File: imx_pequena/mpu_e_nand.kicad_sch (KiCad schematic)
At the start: 1 part, among them U1 MCIMX6Z0DVM09AB

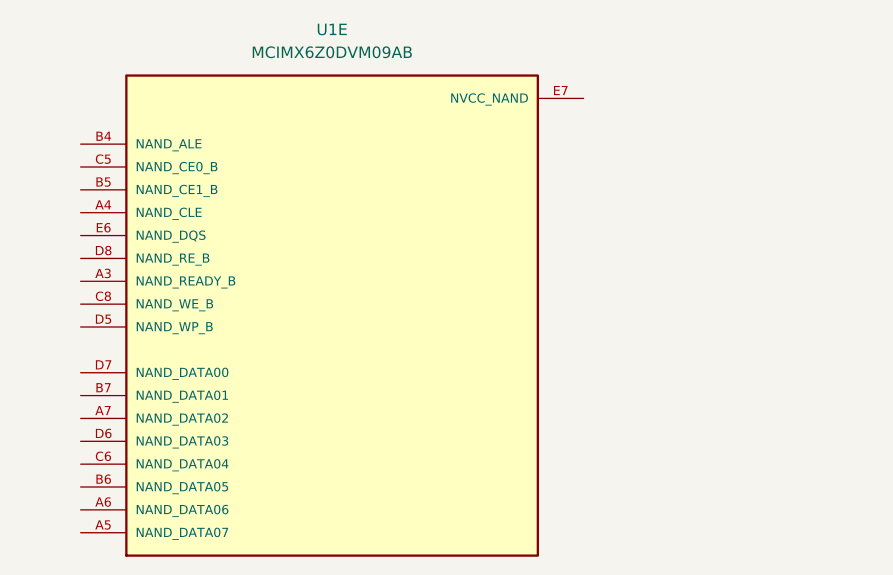
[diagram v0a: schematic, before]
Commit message: Cleaned up NVCC pins
Added 3v3 connections + decoupling caps to NVcc pins
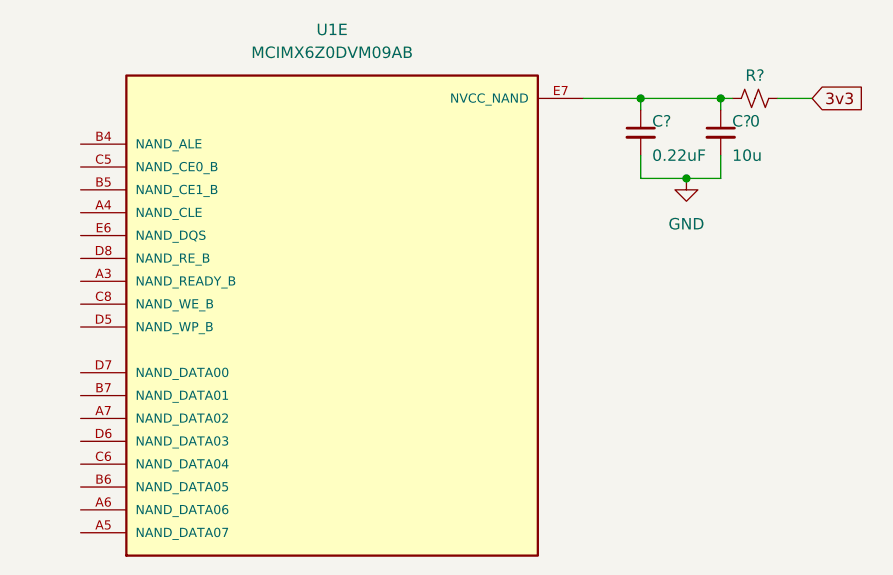
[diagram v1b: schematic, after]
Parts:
- added C?: 10u, symbol Device:C_Small
- added C?: 0.22uF, symbol Device:C_Small
- added R?: 0, symbol Device:R_Small_US
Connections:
- net at U1.E7 (NVCC_NAND): now also C?.1, C?.1, R?.1
- new net 3v3: R?.2
- new net GND: C?.2, C?.2
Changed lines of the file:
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@@
 (kicad_sch (version 20211123) (generator eeschema)
   (paper "A4")
+  (junction (at 181.61 63.5) (diameter 0) (color 0 0 0 0)
+  )
+  (junction (at 190.5 63.5) (diameter 0) (color 0 0 0 0)
+  )
+  (junction (at 186.69 72.39) (diameter 0) (color 0 0 0 0)
+  )
+  (wire (pts (xy 190.5 69.85) (xy 190.5 72.39))
+    (stroke (width 0) (type default) (color 0 0 0 0))
+  )
+  (wire (pts (xy 190.5 63.5) (xy 191.77 63.5))
+    (stroke (width 0) (type default) (color 0 0 0 0))
+  )
+  (wire (pts (xy 190.5 63.5) (xy 190.5 64.77))
+    (stroke (width 0) (type default) (color 0 0 0 0))
+  )
+  (wire (pts (xy 181.61 63.5) (xy 181.61 64.77))
+    (stroke (width 0) (type default) (color 0 0 0 0))
+  )
+  (wire (pts (xy 181.61 63.5) (xy 190.5 63.5))
+    (stroke (width 0) (type default) (color 0 0 0 0))
+  )
+  (wire (pts (xy 175.26 63.5) (xy 181.61 63.5))
+    (stroke (width 0) (type default) (color 0 0 0 0))
+  )
+  (wire (pts (xy 186.69 72.39) (xy 190.5 72.39))
+    (stroke (width 0) (type default) (color 0 0 0 0))
+  )
+  (wire (pts (xy 181.61 72.39) (xy 186.69 72.39))
+    (stroke (width 0) (type default) (color 0 0 0 0))
+  )
+  (wire (pts (xy 196.85 63.5) (xy 200.66 63.5))
+    (stroke (width 0) (type default) (color 0 0 0 0))
+  )
+  (wire (pts (xy 181.61 69.85) (xy 181.61 72.39))
+    (stroke (width 0) (type default) (color 0 0 0 0))
+  )
+  (global_label "3v3" (shape input) (at 200.66 63.5 0) (fields_autoplaced)
+    (effects (font (size 1.27 1.27)) (justify left))
+    (property "Intersheet References" "${INTERSHEET_REFS}" (id 0) (at 206.4598 63.4206 0)
+      (effects (font (size 1.27 1.27)) (justify left) hide)
+    )
+  )
+  (symbol (lib_id "Device:C_Small") (at 190.5 67.31 0) (unit 1)
+    (in_bom yes) (on_board yes)
+    (property "Reference" "C?" (id 0) (at 191.77 66.04 0)
+      (effects (font (size 1.27 1.27)) (justify left))
+    )
+    (property "Value" "10u" (id 1) (at 191.77 69.85 0)
+      (effects (font (size 1.27 1.27)) (justify left))
+    )
+    (property "Footprint" "" (id 2) (at 190.5 67.31 0)
+      (effects (font (size 1.27 1.27)) hide)
+    )
+    (property "Datasheet" "~" (id 3) (at 190.5 67.31 0)
+      (effects (font (size 1.27 1.27)) hide)
+    )
+    (pin "1")
+    (pin "2")
+  )
+  (symbol (lib_id "Device:R_Small_US") (at 194.31 63.5 90) (unit 1)
+    (in_bom yes) (on_board yes)
+    (property "Reference" "R?" (id 0) (at 194.31 60.96 90))
+    (property "Value" "0" (id 1) (at 194.31 66.04 90))
+    (property "Footprint" "" (id 2) (at 194.31 63.5 0)
+      (effects (font (size 1.27 1.27)) hide)
+    )
+    (property "Datasheet" "~" (id 3) (at 194.31 63.5 0)
+      (effects (font (size 1.27 1.27)) hide)
+    )
+    (pin "1")
+    (pin "2")
+  )
+  (symbol (lib_id "power:GND") (at 186.69 72.39 0) (unit 1)
+    (in_bom yes) (on_board yes) (fields_autoplaced)
+    (property "Reference" "#PWR?" (id 0) (at 186.69 78.74 0)
+      (effects (font (size 1.27 1.27)) hide)
+    )
+    (property "Value" "GND" (id 1) (at 186.69 77.47 0))
+    (property "Footprint" "" (id 2) (at 186.69 72.39 0)
+      (effects (font (size 1.27 1.27)) hide)
+    )
+    (property "Datasheet" "" (id 3) (at 186.69 72.39 0)
+      (effects (font (size 1.27 1.27)) hide)
+    )
+    (pin "1")
+  )
   (symbol (lib_id "MCIMX6Z0DVM09AB:MCIMX6Z0DVM09AB") (at 147.32 86.36 0) (unit 5)
     (in_bom yes) (on_board yes) (fields_autoplaced)
@@
     (pin "E7")
   )
+  (symbol (lib_id "Device:C_Small") (at 181.61 67.31 0) (unit 1)
+    (in_bom yes) (on_board yes)
+    (property "Reference" "C?" (id 0) (at 182.88 66.04 0)
+      (effects (font (size 1.27 1.27)) (justify left))
+    )
+    (property "Value" "0.22uF" (id 1) (at 182.88 69.85 0)
+      (effects (font (size 1.27 1.27)) (justify left))
+    )
+    (property "Footprint" "" (id 2) (at 181.61 67.31 0)
+      (effects (font (size 1.27 1.27)) hide)
+    )
+    (property "Datasheet" "~" (id 3) (at 181.61 67.31 0)
+      (effects (font (size 1.27 1.27)) hide)
+    )
+    (pin "1")
+    (pin "2")
+  )
 )

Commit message: Updated pinouts
Added misc uart changes
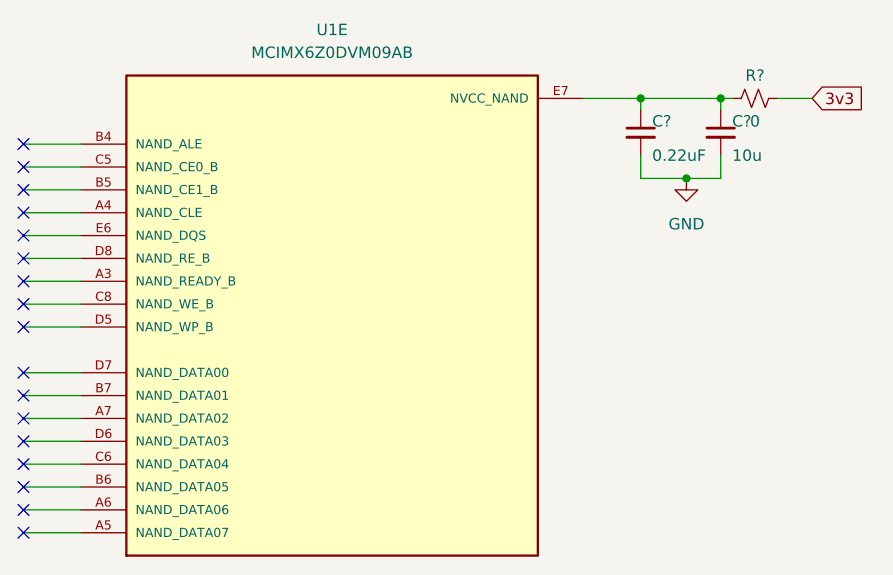
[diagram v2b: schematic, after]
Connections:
- no-connect marks 0 -> 17
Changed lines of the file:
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@@
   (junction (at 186.69 72.39) (diameter 0) (color 0 0 0 0)
   )
+  (no_connect (at 113.03 76.2))
+  (no_connect (at 113.03 99.06))
+  (no_connect (at 113.03 109.22))
+  (no_connect (at 113.03 88.9))
+  (no_connect (at 113.03 81.28))
+  (no_connect (at 113.03 106.68))
+  (no_connect (at 113.03 96.52))
+  (no_connect (at 113.03 104.14))
+  (no_connect (at 113.03 73.66))
+  (no_connect (at 113.03 68.58))
+  (no_connect (at 113.03 71.12))
+  (no_connect (at 113.03 93.98))
+  (no_connect (at 113.03 111.76))
+  (no_connect (at 113.03 78.74))
+  (no_connect (at 113.03 101.6))
+  (no_connect (at 113.03 86.36))
+  (no_connect (at 113.03 83.82))
   (wire (pts (xy 190.5 69.85) (xy 190.5 72.39))
     (stroke (width 0) (type default) (color 0 0 0 0))
@@
     (stroke (width 0) (type default) (color 0 0 0 0))
   )
+  (wire (pts (xy 113.03 99.06) (xy 119.38 99.06))
+    (stroke (width 0) (type default) (color 0 0 0 0))
+  )
+  (wire (pts (xy 113.03 86.36) (xy 119.38 86.36))
+    (stroke (width 0) (type default) (color 0 0 0 0))
+  )
   (wire (pts (xy 190.5 63.5) (xy 190.5 64.77))
+    (stroke (width 0) (type default) (color 0 0 0 0))
+  )
+  (wire (pts (xy 113.03 83.82) (xy 119.38 83.82))
     (stroke (width 0) (type default) (color 0 0 0 0))
   )
@@
     (stroke (width 0) (type default) (color 0 0 0 0))
   )
+  (wire (pts (xy 113.03 73.66) (xy 119.38 73.66))
+    (stroke (width 0) (type default) (color 0 0 0 0))
+  )
+  (wire (pts (xy 113.03 88.9) (xy 119.38 88.9))
+    (stroke (width 0) (type default) (color 0 0 0 0))
+  )
   (wire (pts (xy 181.61 63.5) (xy 190.5 63.5))
+    (stroke (width 0) (type default) (color 0 0 0 0))
+  )
+  (wire (pts (xy 113.03 68.58) (xy 119.38 68.58))
+    (stroke (width 0) (type default) (color 0 0 0 0))
+  )
+  (wire (pts (xy 113.03 96.52) (xy 119.38 96.52))
     (stroke (width 0) (type default) (color 0 0 0 0))
   )
@@
     (stroke (width 0) (type default) (color 0 0 0 0))
   )
+  (wire (pts (xy 113.03 111.76) (xy 119.38 111.76))
+    (stroke (width 0) (type default) (color 0 0 0 0))
+  )
+  (wire (pts (xy 113.03 78.74) (xy 119.38 78.74))
+    (stroke (width 0) (type default) (color 0 0 0 0))
+  )
+  (wire (pts (xy 113.03 71.12) (xy 119.38 71.12))
+    (stroke (width 0) (type default) (color 0 0 0 0))
+  )
+  (wire (pts (xy 113.03 93.98) (xy 119.38 93.98))
+    (stroke (width 0) (type default) (color 0 0 0 0))
+  )
+  (wire (pts (xy 113.03 101.6) (xy 119.38 101.6))
+    (stroke (width 0) (type default) (color 0 0 0 0))
+  )
   (wire (pts (xy 181.61 72.39) (xy 186.69 72.39))
+    (stroke (width 0) (type default) (color 0 0 0 0))
+  )
+  (wire (pts (xy 113.03 81.28) (xy 119.38 81.28))
     (stroke (width 0) (type default) (color 0 0 0 0))
   )
@@
     (stroke (width 0) (type default) (color 0 0 0 0))
   )
+  (wire (pts (xy 113.03 109.22) (xy 119.38 109.22))
+    (stroke (width 0) (type default) (color 0 0 0 0))
+  )
+  (wire (pts (xy 113.03 76.2) (xy 119.38 76.2))
+    (stroke (width 0) (type default) (color 0 0 0 0))
+  )
   (wire (pts (xy 181.61 69.85) (xy 181.61 72.39))
     (stroke (width 0) (type default) (color 0 0 0 0))
   )
+  (wire (pts (xy 113.03 104.14) (xy 119.38 104.14))
+    (stroke (width 0) (type default) (color 0 0 0 0))
+  )
+  (wire (pts (xy 113.03 106.68) (xy 119.38 106.68))
+    (stroke (width 0) (type default) (color 0 0 0 0))
+  )

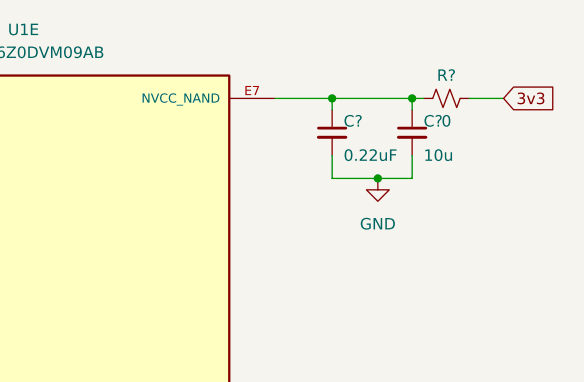
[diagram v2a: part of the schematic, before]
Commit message: Part Assignment
Assigned GPIOs and assigned footprints to most parts
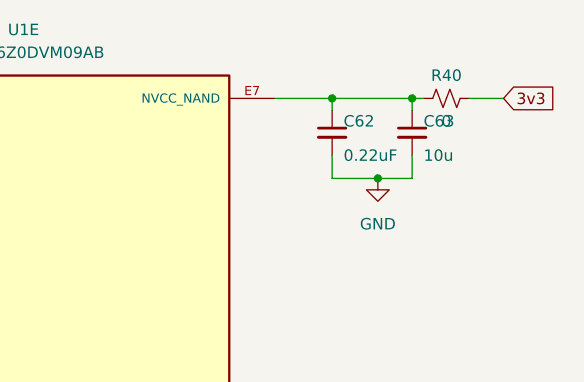
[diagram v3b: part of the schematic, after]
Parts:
- C62: renamed from C?; footprint (none) -> Capacitor_SMD:C_0402_1005Metric
- C63: renamed from C?; footprint (none) -> Capacitor_SMD:C_0805_2012Metric
- R40: renamed from R?; footprint (none) -> Resistor_SMD:R_0402_1005Metric
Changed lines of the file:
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@@
   (symbol (lib_id "Device:C_Small") (at 190.5 67.31 0) (unit 1)
     (in_bom yes) (on_board yes)
-    (property "Reference" "C?" (id 0) (at 191.77 66.04 0)
+    (property "Reference" "C63" (id 0) (at 191.77 66.04 0)
       (effects (font (size 1.27 1.27)) (justify left))
     )
@@
       (effects (font (size 1.27 1.27)) (justify left))
     )
-    (property "Footprint" "" (id 2) (at 190.5 67.31 0)
+    (property "Footprint" "Capacitor_SMD:C_0805_2012Metric" (id 2) (at 190.5 67.31 0)
       (effects (font (size 1.27 1.27)) hide)
     )
@@
   (symbol (lib_id "Device:R_Small_US") (at 194.31 63.5 90) (unit 1)
     (in_bom yes) (on_board yes)
-    (property "Reference" "R?" (id 0) (at 194.31 60.96 90))
+    (property "Reference" "R40" (id 0) (at 194.31 60.96 90))
     (property "Value" "0" (id 1) (at 194.31 66.04 90))
-    (property "Footprint" "" (id 2) (at 194.31 63.5 0)
+    (property "Footprint" "Resistor_SMD:R_0402_1005Metric" (id 2) (at 194.31 63.5 0)
       (effects (font (size 1.27 1.27)) hide)
     )
@@
   (symbol (lib_id "power:GND") (at 186.69 72.39 0) (unit 1)
     (in_bom yes) (on_board yes) (fields_autoplaced)
-    (property "Reference" "#PWR?" (id 0) (at 186.69 78.74 0)
+    (property "Reference" "#PWR0153" (id 0) (at 186.69 78.74 0)
       (effects (font (size 1.27 1.27)) hide)
     )
@@
   (symbol (lib_id "Device:C_Small") (at 181.61 67.31 0) (unit 1)
     (in_bom yes) (on_board yes)
-    (property "Reference" "C?" (id 0) (at 182.88 66.04 0)
+    (property "Reference" "C62" (id 0) (at 182.88 66.04 0)
       (effects (font (size 1.27 1.27)) (justify left))
     )
@@
       (effects (font (size 1.27 1.27)) (justify left))
     )
-    (property "Footprint" "" (id 2) (at 181.61 67.31 0)
+    (property "Footprint" "Capacitor_SMD:C_0402_1005Metric" (id 2) (at 181.61 67.31 0)
       (effects (font (size 1.27 1.27)) hide)
     )
